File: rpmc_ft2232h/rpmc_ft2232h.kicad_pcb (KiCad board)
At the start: 2 copper layers, 60.8 x 58 mm, 4 parts, among them J1 Conn_02x20_Odd_Even, U2 74HC373, U3 74LS139

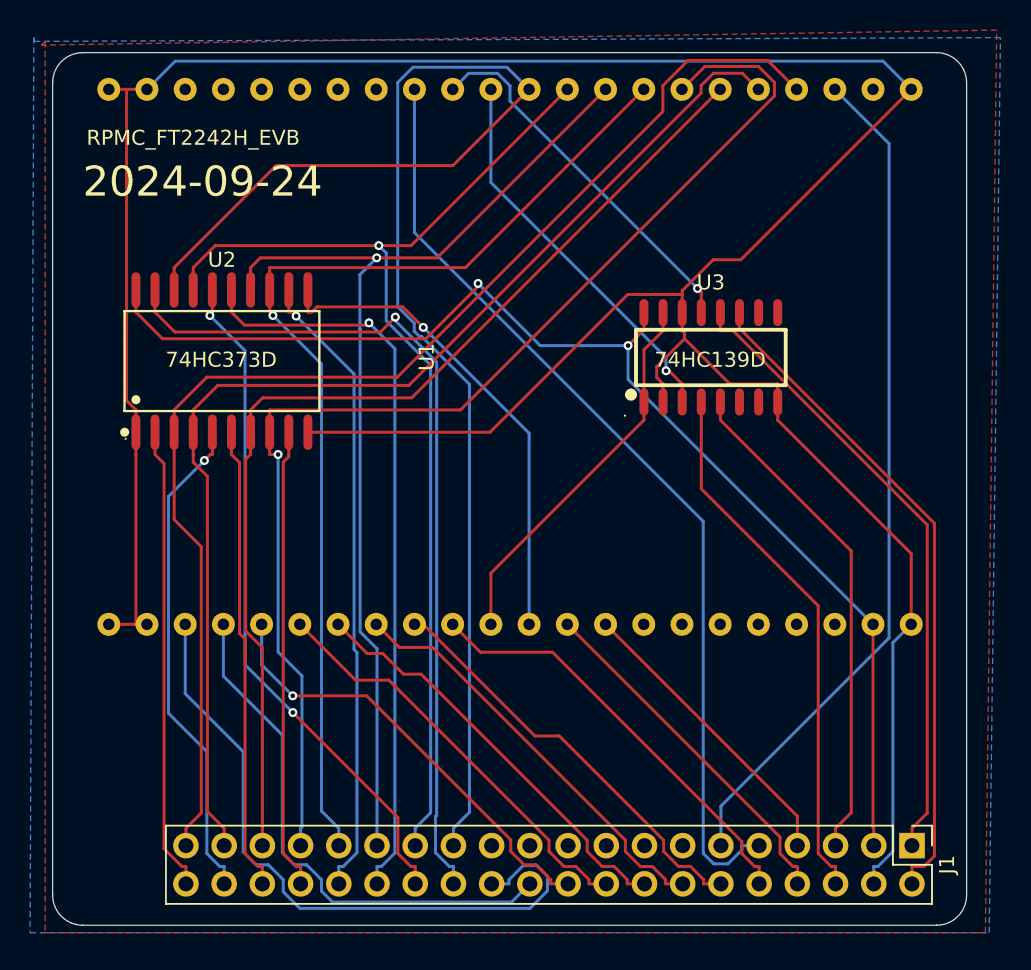
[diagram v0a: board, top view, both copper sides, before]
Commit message: rpmc_ft2232h/rpmc_ft2232h.kicad_pcb rpmc_ft2232h/rpmc_ft2232h.kicad_sch
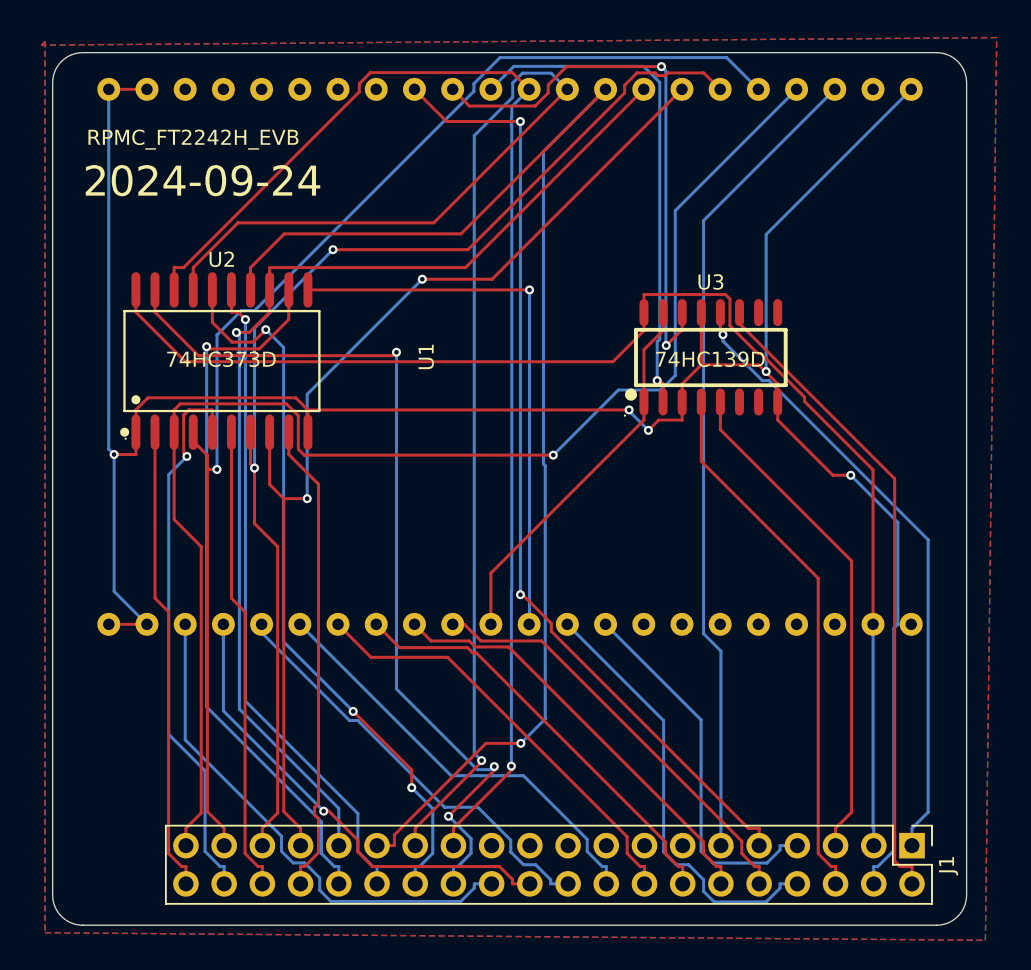
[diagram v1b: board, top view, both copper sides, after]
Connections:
- U3 pad 13: /SLT -> GND
- U3 pad 14: GND -> /SLT
- U3 pad 2: GND -> /M_IO
- U3 pad 3: /M_IO -> GND
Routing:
- net GND: track 196.6 -> 160.5 mm, vias 0 -> 5
- net /D5: track 70.0 -> 88.7 mm
- net /D6: track 73.0 -> 89.4 mm
- net /SLT: track 24.9 -> 37.1 mm, vias 1 -> 2
- net /A8: track 45.1 -> 34.2 mm
- net /D3: track 80.5 -> 70.1 mm, vias 1 -> 2
- net /D7: track 93.0 -> 83.6 mm, vias 0 -> 1
- net /D0: track 82.9 -> 90.9 mm, vias 0 -> 1
- net /M_IO: track 26.2 -> 33.9 mm
- net /D2: track 69.6 -> 76.8 mm, vias 0 -> 2
- net /A5: track 49.7 -> 43.9 mm
- net /A4: track 42.2 -> 47.8 mm
- net /RD: track 23.8 -> 29.2 mm
- net /D1: track 77.4 -> 82.7 mm, vias 0 -> 1
- net /+5V: track 80.9 -> 86.1 mm, vias 2 -> 0
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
